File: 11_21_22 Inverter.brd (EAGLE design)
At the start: 100 x 80 mm, 32 parts, among them IC1 FAN73895MX, Q1 ROHM_SCT3022ALGC11ROHM_SCT302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, Q2 ROHM_SCT3022ALGC11ROHM_SCT302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, Q3 ROHM_SCT3022ALGC11ROHM_SCT302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, Q4 ROHM_SCT3022ALGC11ROHM_SCT302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, Q5 ROHM_SCT3022ALGC11ROHM_SCT302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, Q6 ROHM_SCT3022ALGC11ROHM_SCT302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, U1 RASPBERRY_PICOTH

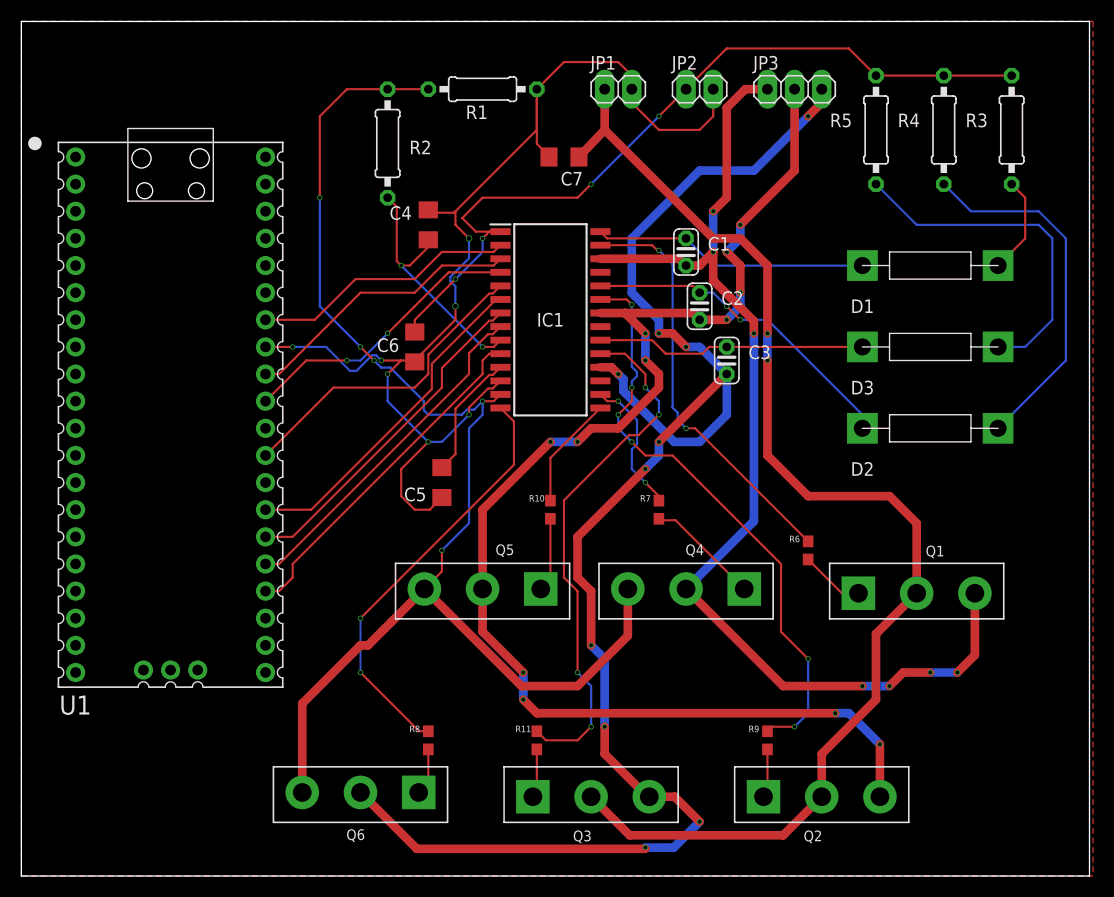
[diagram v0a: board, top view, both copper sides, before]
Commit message: Updated inverter board and schematic with new IC
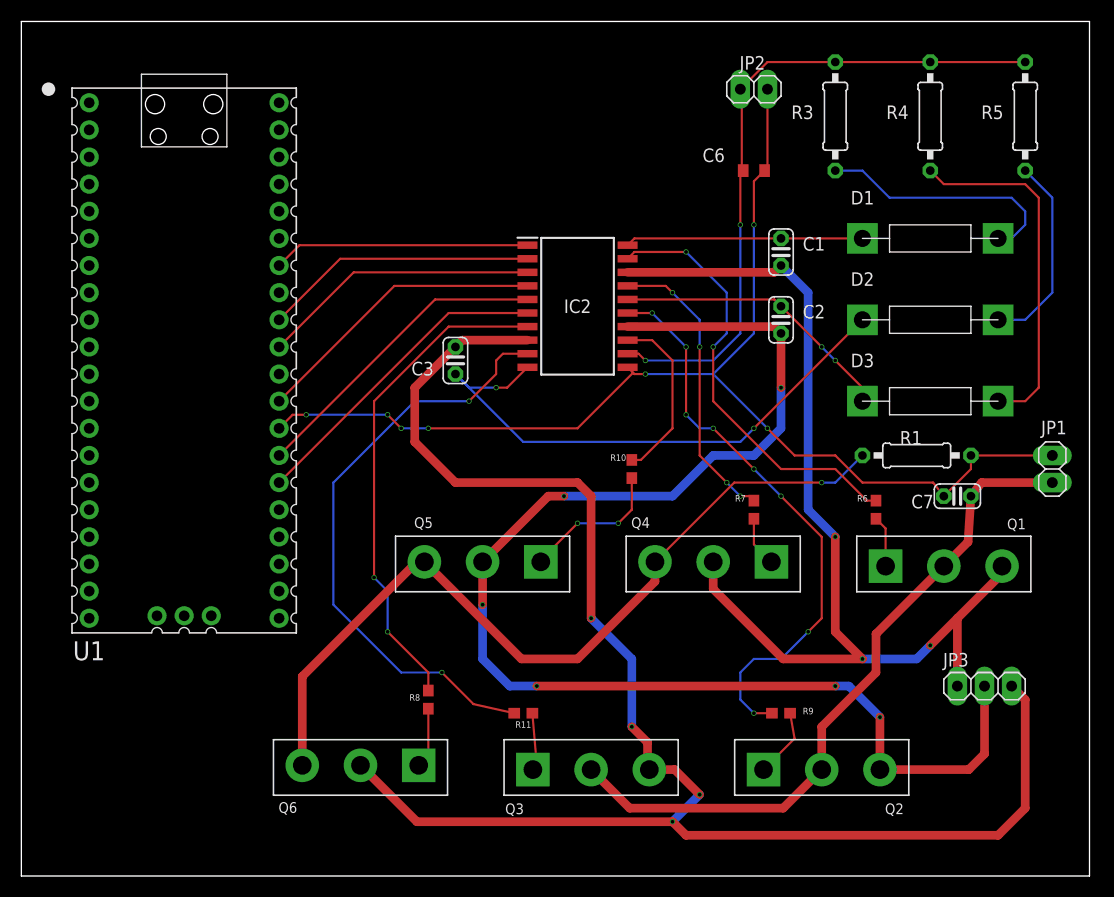
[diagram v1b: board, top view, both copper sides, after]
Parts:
- removed C4: 10n, rcl:C1206
- removed C5: 2n, rcl:C1206
- removed IC1: FAN73895MX, FAN73895MX:SOIC127P1031X265-28N
- removed R2: 1M, rcl:0207/10
- added IC2: FAN7388MX, FAN7388MX:SOIC127P1032X265-20N
- C1, C2, C3: value 8n -> 10n
- C6: value 80n -> 100n; device rcl:C1206 -> rcl:SMC_Z
- C7: value 80n -> 100n; device rcl:C1206 -> rcl:C025-024X044
- moved JP3 58.6 mm to (88.9, 17.8)
- moved JP1 54.0 mm to (95.2, 38.1), turned to 90 degrees
- moved R1 53.2 mm to (82.5, 39.4)
- moved C7 48.6 mm to (86.4, 35.6)
- moved C6 35.8 mm to (67.3, 66.0), turned to 0 degrees
- moved C3 25.4 mm to (39.4, 48.3), turned to 90 degrees
- moved R3 16.6 mm to (74.9, 71.1)
- moved R5 14.0 mm to (92.7, 71.1)
- moved D2 10.2 mm to (76.2, 52.1)
- moved R7 8.89 mm to (67.3, 34.3)
- moved C1 8.89 mm to (69.8, 58.4)
- moved R10 8.52 mm to (55.9, 38.1)
- moved C2 7.73 mm to (69.8, 52.1)
- moved R6 7.41 mm to (78.7, 34.3)
- moved U1 5.24 mm to (14.0, 48.3)
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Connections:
- removed net GND: C4.2, C5.2, C6.2, C7.2, IC1.12, JP1.2, JP2.2, R1.1, U1.13, U1.18, U1.23, U1.28, U1.3, U1.33, U1.38, U1.8
- removed net N$13: IC1.23, R9.1
- removed net N$15: IC1.15, R10.1
- removed net N$17: C1.1, D1.1, IC1.28
- removed net N$18: C2.1, D2.1, IC1.24
- removed net N$19: C3.1, D3.1, IC1.20
- removed net N$20: IC1.3, U1.32
- removed net N$21: C5.1, IC1.11
- removed net N$22: IC1.4, U1.31
- removed net N$23: IC1.5, U1.29
- removed net N$24: IC1.6, U1.27
- removed net N$25: IC1.7, U1.26
- removed net N$27: C4.1, IC1.9, R2.2
- removed net VOUT1: C1.2, IC1.26, JP3.1, Q1.3, Q4.2
- removed net VOUT2: C2.2, IC1.22, JP3.2, Q2.3, Q5.2
- removed net VOUT3: C3.2, IC1.18, JP3.3, Q3.3, Q6.2
- new net COM/GND: Q4.3, Q5.3, Q6.3, R1.2
- new net GND1: C6.-, C7.2, IC2.11, JP1.2, JP2.2, R1.1, U1.13, U1.18, U1.23, U1.28, U1.3, U1.33, U1.38, U1.8
- new net HO1: IC2.19, R6.1
- new net HO2: IC2.15, R9.1
- new net LO2: IC2.13, R10.1
- new net LO3: IC2.7, R8.1
- new net VB1: C1.1, D1.1, IC2.20
- new net VB2: C2.1, D3.1, IC2.16
- new net VB3: C3.1, D2.1, IC2.10
- new net VOUT3/VS3: C3.2, IC2.8, JP3.3, Q3.3, Q6.2
- new net VS1/VOUT1: C1.2, IC2.18, JP3.1, Q1.3, Q4.2
- new net VS2/VOUT2: C2.2, IC2.14, JP3.2, Q2.3, Q5.2
- net N$1: now also IC2.1; no longer IC1.2
- net N$12: now also IC2.9, R11.1; no longer IC1.10, U1.24
- net N$2: now also IC2.17, R7.1; no longer IC1.13, Q4.3, Q5.3, Q6.3, R1.2, R2.1
- net N$28: now also D3.2; no longer D2.2
- net N$29: now also D2.2; no longer D3.2
- net N$3: now also IC2.2, U1.32; no longer IC1.19, R11.1
- net N$4: now also IC2.3, U1.31; no longer IC1.27, R6.1
- net N$5: now also IC2.4, U1.29; no longer IC1.8, U1.25
- net N$7: now also IC2.5, U1.27; no longer IC1.16, R7.1
- net N$9: now also IC2.6, U1.26; no longer IC1.14, R8.1
- net VDD: now also C6.+, IC2.12; no longer C6.1, IC1.1
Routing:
- net VOUT3: track 151.4 -> 0.00 mm, vias 10 -> 0
- net VOUT3/VS3: track 0.00 -> 151.3 mm, vias 0 -> 4
- net VS2/VOUT2: track 0.00 -> 126.8 mm, vias 0 -> 6
- net VOUT2: track 126.3 -> 0.00 mm, vias 12 -> 0
- net GND1: track 0.00 -> 112.3 mm, vias 0 -> 7
- net GND: track 112.2 -> 0.00 mm, vias 7 -> 0
- net VOUT1: track 103.5 -> 0.00 mm, vias 7 -> 0
- net VS1/VOUT1: track 0.00 -> 97.3 mm, vias 0 -> 3
- net N$2: track 124.6 -> 27.6 mm, vias 5 -> 4
- net COM/GND: track 0.00 -> 77.9 mm, vias 0 -> 1
- net N$13: track 55.7 -> 0.00 mm, vias 6 -> 0
- net HO2: track 0.00 -> 53.9 mm, vias 0 -> 8
- net VB3: track 0.00 -> 53.5 mm, vias 0 -> 2
- net V+: track 116.1 -> 64.1 mm, vias 2 -> 0
- net LO3: track 0.00 -> 46.4 mm, vias 0 -> 2
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- removed copper zone on layer 1, net GND
